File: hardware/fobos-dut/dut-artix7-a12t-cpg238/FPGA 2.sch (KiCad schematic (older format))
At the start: 7 parts, among them U1 XC7A12T-CPG238

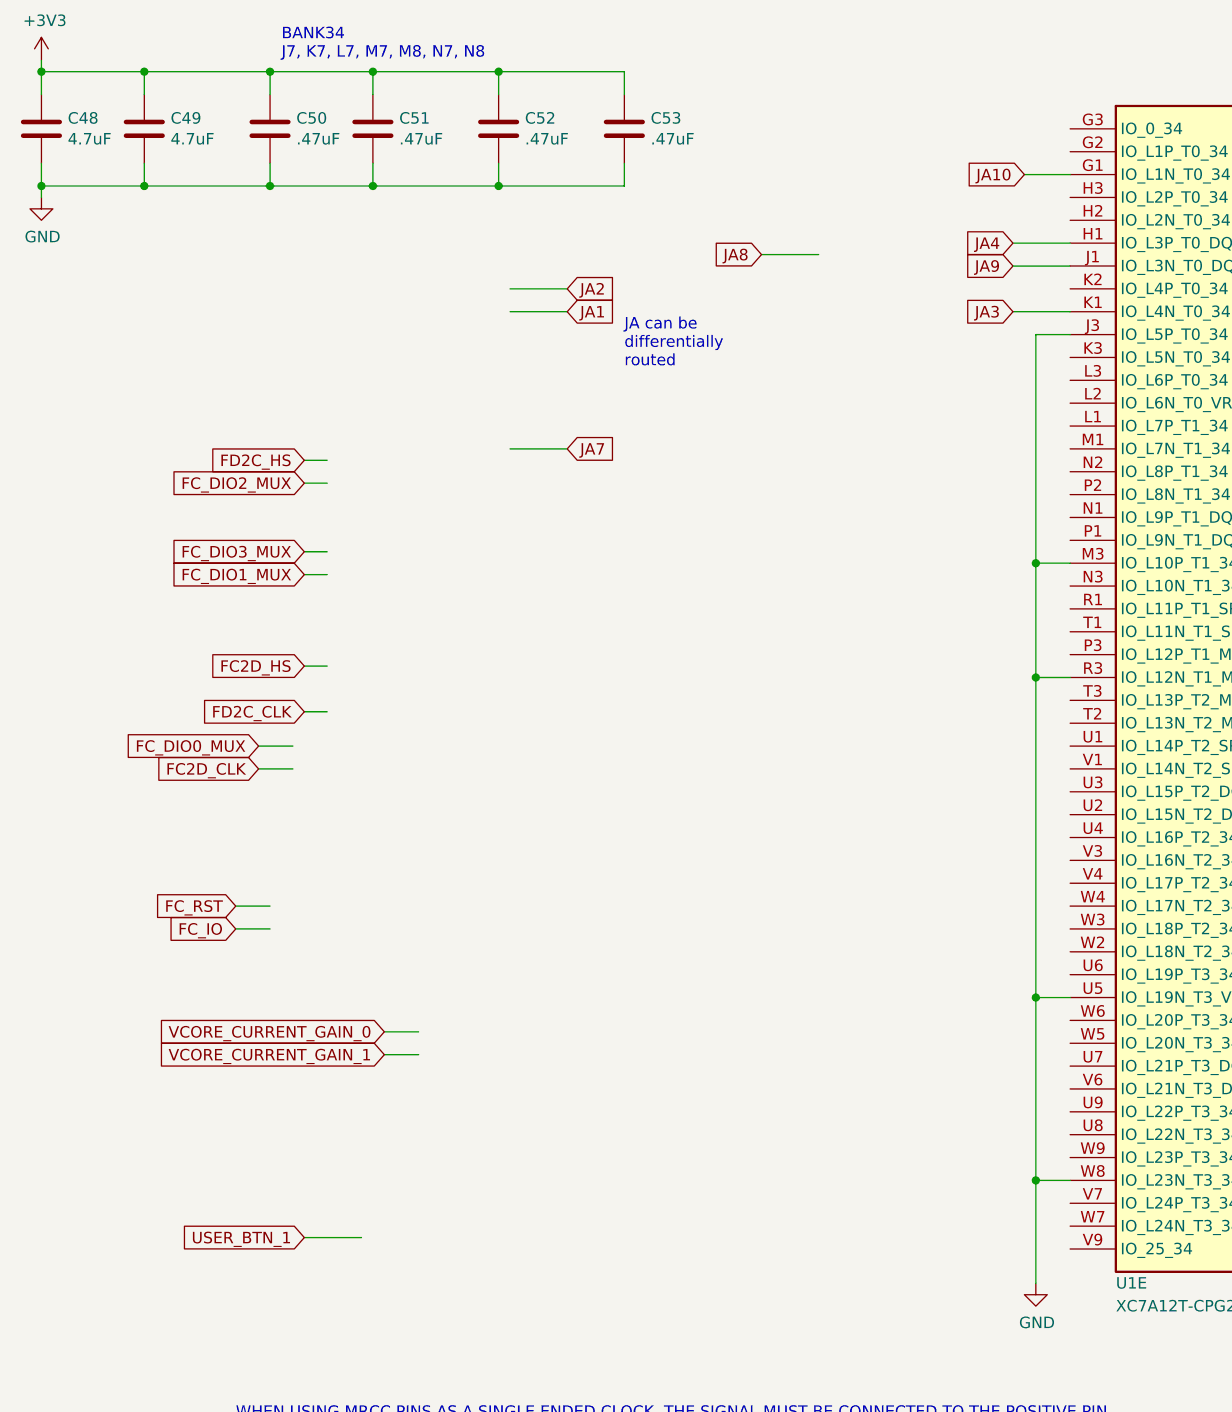
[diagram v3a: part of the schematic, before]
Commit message: All signals routed, need to route power
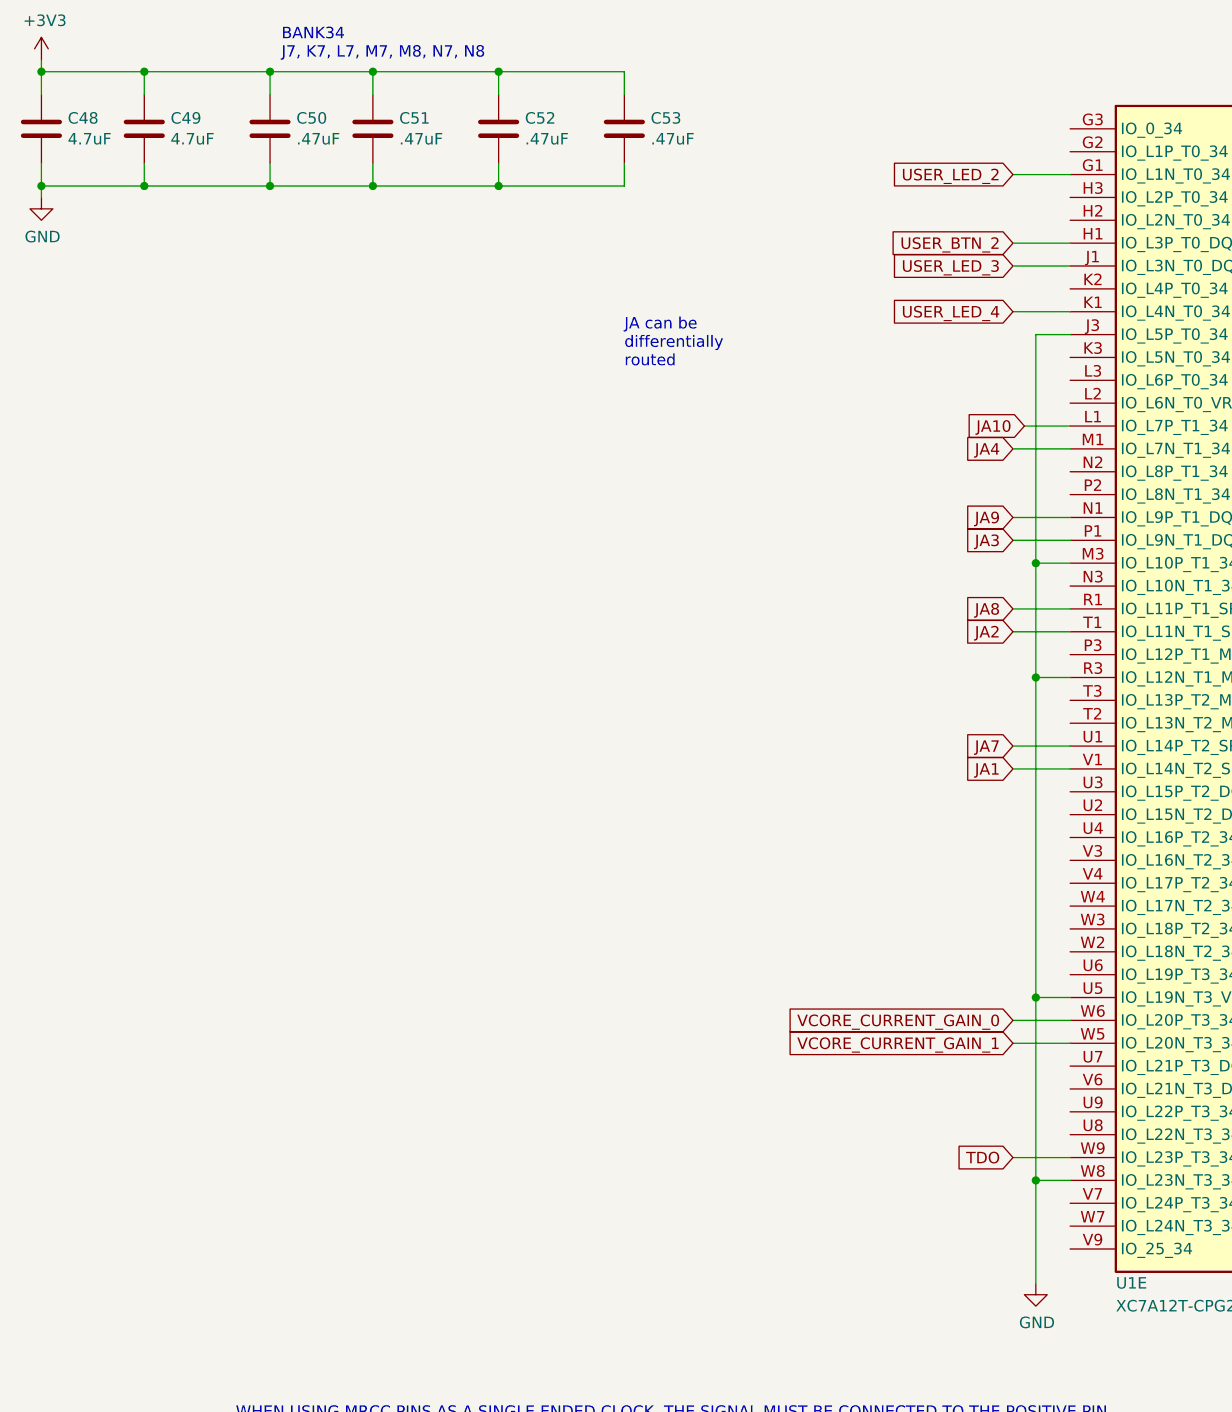
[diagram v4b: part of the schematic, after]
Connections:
- net labels added: TDO, USER_BTN_2, USER_LED_2, USER_LED_3, USER_LED_4
- net labels removed: FC2D_CLK, FC2D_HS, FC_DIO0_MUX, FC_DIO1_MUX, FC_DIO2_MUX, FC_DIO3_MUX, FC_IO, FC_RST, FD2C_CLK, FD2C_HS, USER_BTN_1
- wire segments 68 -> 62
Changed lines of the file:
@@
 	1    0    0    -1
 $EndComp
-Text GLabel 2250 5200 0    50   Input ~ 0
+Text GLabel 5000 5150 0    50   Input ~ 0
 VCORE_CURRENT_GAIN_0
-Text GLabel 2250 5300 0    50   Input ~ 0
+Text GLabel 5000 5250 0    50   Input ~ 0
 VCORE_CURRENT_GAIN_1
-Wire Wire Line
-	2400 5300 2250 5300
-Wire Wire Line
-	2400 5200 2250 5200
-Text GLabel 1900 6100 0    50   Input ~ 0
-USER_BTN_1
-Wire Wire Line
-	1900 6100 2150 6100
-Text GLabel 1900 3100 0    50   Input ~ 0
-FC_DIO3_MUX
-Text GLabel 1700 3950 0    50   Input ~ 0
-FC_DIO0_MUX
-Wire Wire Line
-	1700 3950 1850 3950
-Wire Wire Line
-	1900 3100 2000 3100
-Text GLabel 1600 4650 0    50   Input ~ 0
-FC_RST
-Text GLabel 1600 4750 0    50   Input ~ 0
-FC_IO
-Wire Wire Line
-	1600 4750 1750 4750
-Wire Wire Line
-	1750 4650 1600 4650
-Text GLabel 1900 3200 0    50   Input ~ 0
-FC_DIO1_MUX
-Wire Wire Line
-	1900 3200 2000 3200
-Text GLabel 1900 3600 0    50   Input ~ 0
-FC2D_HS
-Wire Wire Line
-	2000 3600 1900 3600
-Text GLabel 1700 4050 0    50   Input ~ 0
-FC2D_CLK
-Wire Wire Line
-	1850 4050 1700 4050
-Text GLabel 1900 3800 0    50   Input ~ 0
-FD2C_CLK
-Wire Wire Line
-	2000 3800 1900 3800
 $Comp
 L cerg:XC7A12T-CPG238 U1
@@
 	1    0    0    -1
 $EndComp
-Wire Wire Line
-	2000 2700 1900 2700
-Text GLabel 1900 2700 0    50   Input ~ 0
-FD2C_HS
-Wire Wire Line
-	1900 2800 2000 2800
-Text GLabel 1900 2800 0    50   Input ~ 0
-FC_DIO2_MUX
 Wire Wire Line
 	7350 950  7350 800
@@
 Text Notes 1600 6900 0    50   ~ 0
 WHEN USING MRCC PINS AS A SINGLE ENDED CLOCK, THE SIGNAL MUST BE CONNECTED TO THE POSITIVE PIN
-Text GLabel 3050 2050 2    50   Input ~ 0
+Text GLabel 5000 4050 0    50   Input ~ 0
 JA1
-Text GLabel 3050 2650 2    50   Input ~ 0
+Text GLabel 5000 3950 0    50   Input ~ 0
 JA7
-Text GLabel 3050 1950 2    50   Input ~ 0
+Text GLabel 5000 3450 0    50   Input ~ 0
 JA2
-Text GLabel 3900 1800 0    50   Input ~ 0
+Text GLabel 5000 3350 0    50   Input ~ 0
 JA8
-Text GLabel 5000 2050 0    50   Input ~ 0
+Text GLabel 5000 3050 0    50   Input ~ 0
 JA3
-Text GLabel 5000 1850 0    50   Input ~ 0
+Text GLabel 5000 2950 0    50   Input ~ 0
 JA9
-Text GLabel 5000 1750 0    50   Input ~ 0
+Text GLabel 5000 2650 0    50   Input ~ 0
 JA4
 Wire Wire Line
-	3050 2050 2800 2050
-Wire Wire Line
-	2800 2650 3050 2650
-Wire Wire Line
-	2800 1950 3050 1950
-Wire Wire Line
-	3900 1800 4150 1800
-Wire Wire Line
-	5000 2050 5250 2050
-Wire Wire Line
-	5000 1850 5250 1850
-Wire Wire Line
-	5000 1750 5250 1750
+	5000 4050 5250 4050
+Wire Wire Line
+	5250 3950 5000 3950
+Wire Wire Line
+	5250 3450 5000 3450
+Wire Wire Line
+	5000 3350 5250 3350
+Wire Wire Line
+	5000 3050 5250 3050
+Wire Wire Line
+	5000 2950 5250 2950
+Wire Wire Line
+	5000 2650 5250 2650
 Text Notes 3300 2300 0    50   ~ 0
 JA can be \ndifferentially\nrouted
-Text GLabel 5050 1450 0    50   Input ~ 0
+Text GLabel 5050 2550 0    50   Input ~ 0
 JA10
 Wire Wire Line
-	5050 1450 5250 1450
+	5050 2550 5250 2550
 $Comp
 L power:GND #PWR?
@@
 Wire Wire Line
 	5100 5850 5100 6300
+Text GLabel 5000 5750 0    50   Input ~ 0
+TDO
+Wire Wire Line
+	5250 5750 5000 5750
+Wire Wire Line
+	5250 1850 5000 1850
+Text GLabel 5000 1850 0    50   Input ~ 0
+USER_LED_3
+Wire Wire Line
+	5250 2050 5000 2050
+Text GLabel 5000 2050 0    50   Input ~ 0
+USER_LED_4
+Text GLabel 5000 1750 0    50   Input ~ 0
+USER_BTN_2
+Text GLabel 5000 1450 0    50   Input ~ 0
+USER_LED_2
+Wire Wire Line
+	5250 1750 5000 1750
+Wire Wire Line
+	5250 1450 5000 1450
+Wire Wire Line
+	5000 5150 5250 5150
+Wire Wire Line
+	5000 5250 5250 5250
 $EndSCHEMATC

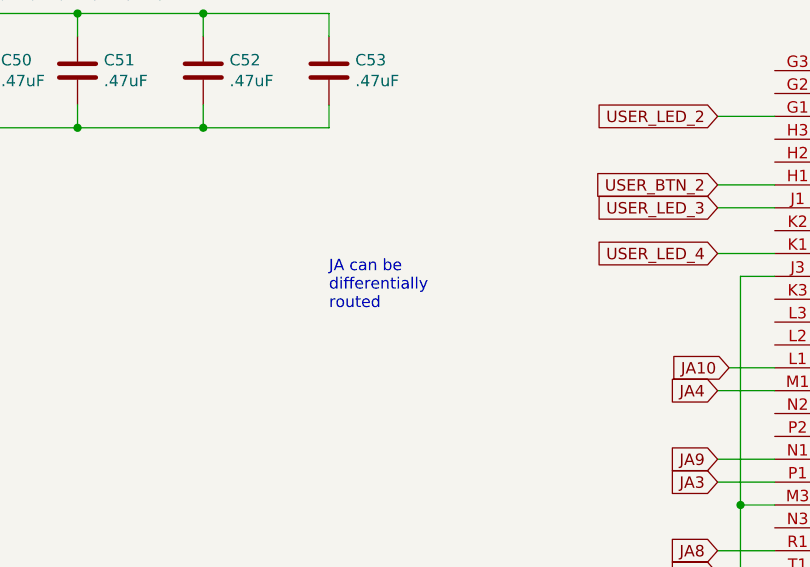
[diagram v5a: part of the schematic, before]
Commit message: Moved PCB so that it fits inside of title block Created BOM which matches the rev 1 design Generated pick and place data, assembly drawings
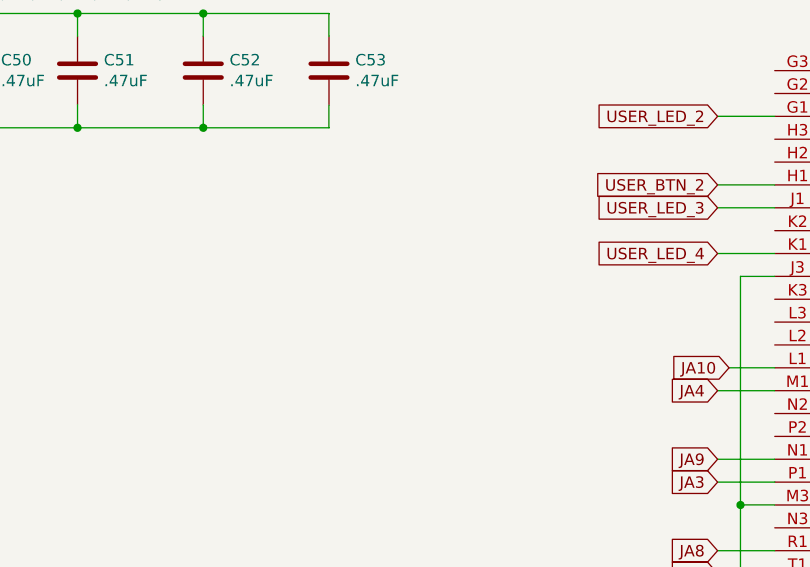
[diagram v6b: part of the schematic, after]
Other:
- note removed: "JA can be \ndifferentially\nrouted"
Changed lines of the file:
@@
 Wire Wire Line
 	5000 2650 5250 2650
-Text Notes 3300 2300 0    50   ~ 0
-JA can be \ndifferentially\nrouted
 Text GLabel 5050 2550 0    50   Input ~ 0
 JA10
